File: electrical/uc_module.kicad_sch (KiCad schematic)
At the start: 36 parts, among them J1 Screw_Terminal_01x01, J6 Conn_01x06_Pin, K2 Starter RELAY, SW2 SW_SPST, SW3 NEUTRAL DETECT, SW4 KILL SWITCH, SW5 STARTER SWITCH, U1 ATtiny84A-PU, U2 LM7905

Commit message: Fixes in power module
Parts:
- removed D2: 1N4001, Diode_THT:D_DO-41_SOD81_P10.16mm_Horizontal, symbol Diode:1N4001
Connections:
- net POWER is gone; now on an unnamed net: F4.1
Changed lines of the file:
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@@
     (date "2023-03-26")
-  )
-  (junction (at 40.64 38.1) (diameter 0) (color 0 0 0 0)
   )
   (junction (at 52.07 124.46) (diameter 0) (color 0 0 0 0)
@@
     (stroke (width 0) (type default))
   )
-  (wire (pts (xy 43.18 49.53) (xy 40.64 49.53))
-    (stroke (width 0) (type default))
-  )
   (wire (pts (xy 68.58 87.63) (xy 77.47 87.63))
     (stroke (width 0) (type default))
@@
     (stroke (width 0) (type default))
   )
-  (wire (pts (xy 40.64 38.1) (xy 39.37 38.1))
+  (wire (pts (xy 29.21 38.1) (xy 50.8 38.1))
     (stroke (width 0) (type default))
   )
@@
     (stroke (width 0) (type default))
   )
-  (wire (pts (xy 40.64 38.1) (xy 40.64 49.53))
-    (stroke (width 0) (type default))
-  )
   (bus (pts (xy 80.01 92.71) (xy 80.01 95.25))
     (stroke (width 0) (type default))
@@
     (stroke (width 0) (type default))
   )
-  (wire (pts (xy 29.21 38.1) (xy 31.75 38.1))
-    (stroke (width 0) (type default))
-  )
   (wire (pts (xy 68.58 77.47) (xy 138.43 77.47))
     (stroke (width 0) (type default))
@@
   )
   (wire (pts (xy 214.63 71.12) (xy 214.63 102.87))
-    (stroke (width 0) (type default))
-  )
-  (wire (pts (xy 40.64 38.1) (xy 50.8 38.1))
     (stroke (width 0) (type default))
   )
@@
   (label "SCK" (at 69.85 87.63 0) (fields_autoplaced)
     (effects (font (size 1.27 1.27)) (justify left bottom))
-  )
-  (global_label "POWER" (shape bidirectional) (at 43.18 49.53 0) (fields_autoplaced)
-    (effects (font (size 1.27 1.27)) (justify left))
-    (property "Intersheetrefs" "${INTERSHEET_REFS}" (at 53.668 49.53 0)
-      (effects (font (size 1.27 1.27)) (justify left) hide)
-    )
   )
   (global_label "BULB STATUS" (shape input) (at 36.83 85.09 180) (fields_autoplaced)
@@
         )
       )
-    )
-  )
-  (symbol (lib_id "Diode:1N4001") (at 35.56 38.1 180) (unit 1)
-    (in_bom yes) (on_board yes) (dnp no)
-    (property "Reference" "D2" (at 35.56 43.18 0)
-      (effects (font (size 1.27 1.27)))
-    )
-    (property "Value" "1N4001" (at 35.56 40.64 0)
-      (effects (font (size 1.27 1.27)))
-    )
-    (property "Footprint" "Diode_THT:D_DO-41_SOD81_P10.16mm_Horizontal" (at 35.56 38.1 0)
-      (effects (font (size 1.27 1.27)) hide)
-    )
-    (property "Datasheet" "http://www.vishay.com/docs/88503/1n4001.pdf" (at 35.56 38.1 0)
-      (effects (font (size 1.27 1.27)) hide)
-    )
-    (property "Sim.Device" "D" (at 35.56 38.1 0)
-      (effects (font (size 1.27 1.27)) hide)
-    )
-    (property "Sim.Pins" "1=K 2=A" (at 35.56 38.1 0)
-      (effects (font (size 1.27 1.27)) hide)
-    )
-    (pin "1")
-    (pin "2")
-    (instances
-      (project "led_drive"
-        (path "/01e69042-7c7e-48e9-b7c3-459316fd17f1/111fb05e-7613-4dff-b0ef-7b688bb51755"
-          (reference "D2") (unit 1)
-        )
-      )

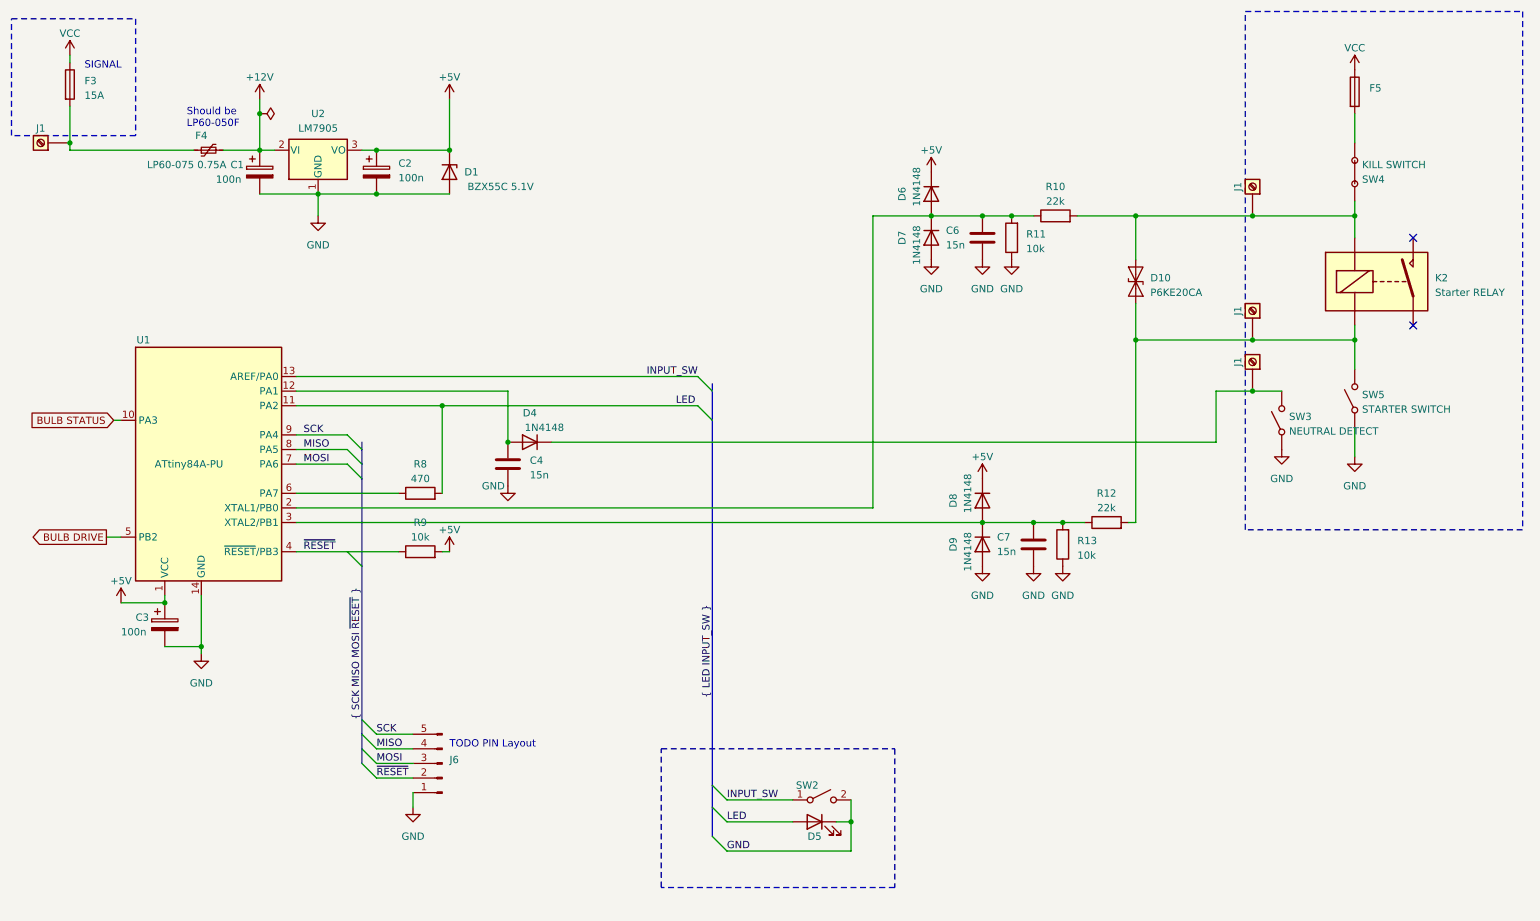
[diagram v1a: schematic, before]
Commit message: Added power module with MOSFET-N
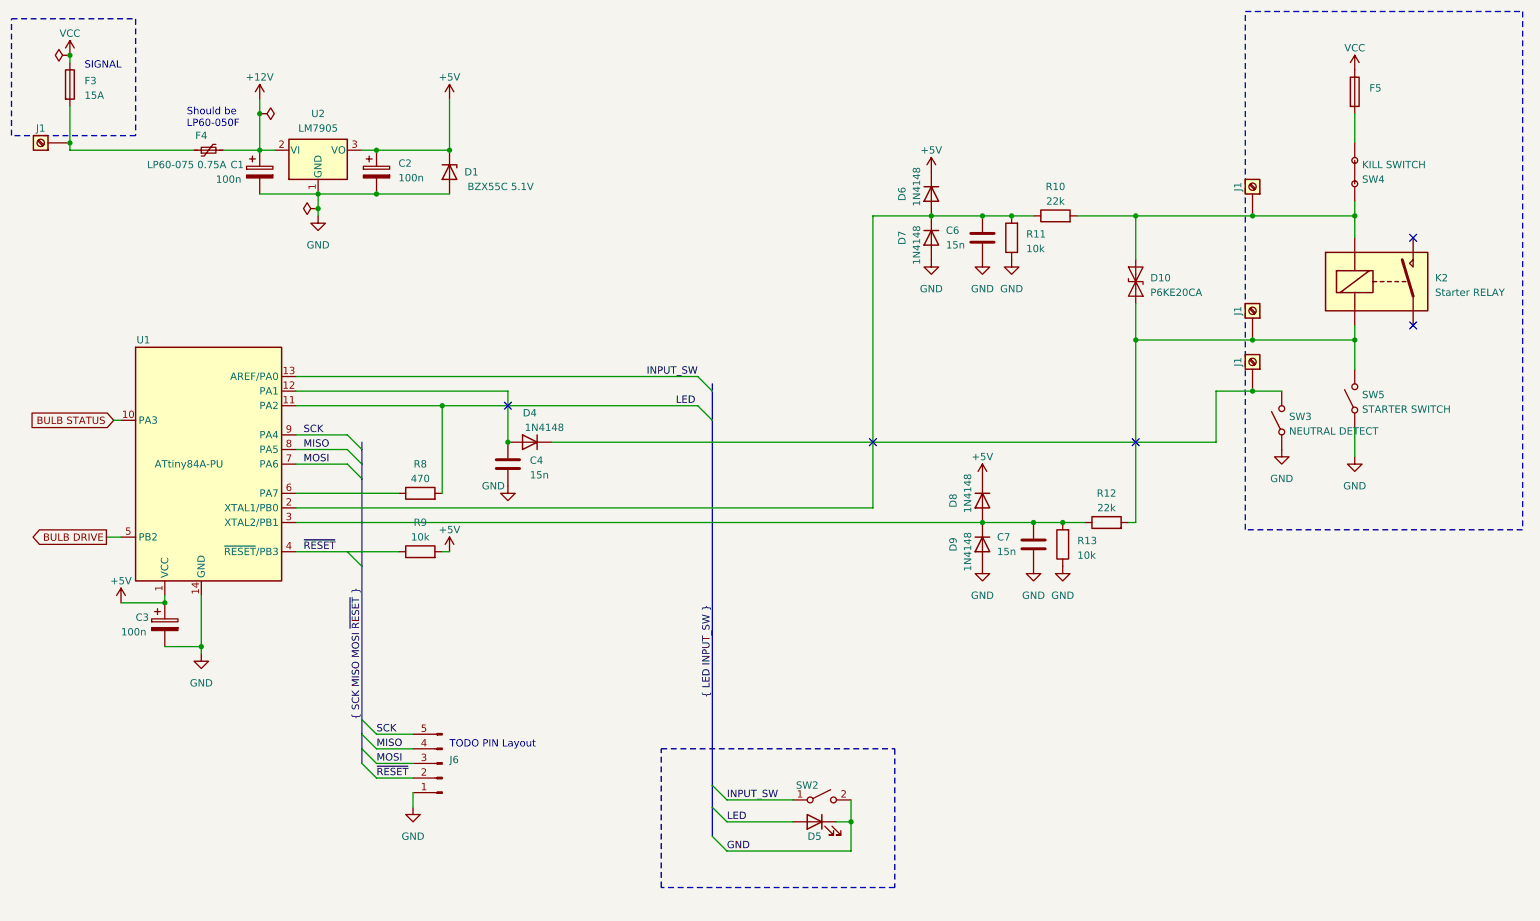
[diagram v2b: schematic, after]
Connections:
- no-connect marks 2 -> 5
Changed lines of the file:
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@@
     (date "2023-03-26")
   )
+  (junction (at 72.39 48.26) (diameter 0) (color 0 0 0 0)
+  )
   (junction (at 52.07 124.46) (diameter 0) (color 0 0 0 0)
   )
@@
   (junction (at 45.72 116.84) (diameter 0) (color 0 0 0 0)
   )
+  (junction (at 29.21 21.59) (diameter 0) (color 0 0 0 0)
+  )
   (junction (at 165.1 154.94) (diameter 0) (color 0 0 0 0)
   )
@@
   )
   (no_connect (at 262.89 53.34))
+  (no_connect (at 105.41 82.55))
+  (no_connect (at 168.91 88.9))
+  (no_connect (at 214.63 88.9))
   (no_connect (at 262.89 68.58))
   (bus_entry (at 80.01 137.16) (size 2.54 2.54)
@@
     (stroke (width 0) (type default))
   )
+  (wire (pts (xy 72.39 48.26) (xy 72.39 45.72))
+    (stroke (width 0) (type default))
+  )
   (wire (pts (xy 36.83 85.09) (xy 38.1 85.09))
     (stroke (width 0) (type default))
@@
     (stroke (width 0) (type default))
   )
-  (wire (pts (xy 72.39 49.53) (xy 72.39 45.72))
+  (wire (pts (xy 72.39 49.53) (xy 72.39 48.26))
     (stroke (width 0) (type default))
   )
@@
     )
   )
+  (symbol (lib_id "power:PWR_FLAG") (at 29.21 21.59 90) (unit 1)
+    (in_bom yes) (on_board yes) (dnp no) (fields_autoplaced)
+    (property "Reference" "#FLG04" (at 27.305 21.59 0)
+      (effects (font (size 1.27 1.27)) hide)
+    )
+    (property "Value" "PWR_FLAG" (at 25.4 22.225 90)
+      (effects (font (size 1.27 1.27)) (justify left) hide)
+    )
+    (property "Footprint" "" (at 29.21 21.59 0)
+      (effects (font (size 1.27 1.27)) hide)
+    )
+    (property "Datasheet" "~" (at 29.21 21.59 0)
+      (effects (font (size 1.27 1.27)) hide)
+    )
+    (property "Sim.Device" "V" (at 29.21 21.59 0)
+      (effects (font (size 1.27 1.27)) hide)
+    )
+    (property "Sim.Type" "DC" (at 29.21 21.59 0)
+      (effects (font (size 1.27 1.27)) hide)
+    )
+    (property "Sim.Pins" "1=+" (at 29.21 21.59 0)
+      (effects (font (size 1.27 1.27)) hide)
+    )
+    (property "Sim.Params" "dc=12" (at 29.21 21.59 0)
+      (effects (font (size 1.27 1.27)) hide)
+    )
+    (pin "1")
+    (instances
+      (project "led_drive"
+        (path "/01e69042-7c7e-48e9-b7c3-459316fd17f1/111fb05e-7613-4dff-b0ef-7b688bb51755"
+          (reference "#FLG04") (unit 1)
+        )
+      )
+    )
+  )
   (symbol (lib_id "power:GND") (at 187.96 110.49 0) (unit 1)
     (in_bom yes) (on_board yes) (dnp no) (fields_autoplaced)
@@
         )
       )
+    )
+  )
+  (symbol (lib_id "power:PWR_FLAG") (at 72.39 48.26 90) (unit 1)
+    (in_bom yes) (on_board yes) (dnp no) (fields_autoplaced)
+    (property "Reference" "#FLG02" (at 70.485 48.26 0)
+      (effects (font (size 1.27 1.27)) hide)
+    )
+    (property "Value" "PWR_FLAG" (at 68.58 48.895 90)
+      (effects (font (size 1.27 1.27)) (justify left) hide)
+    )
+    (property "Footprint" "" (at 72.39 48.26 0)
+      (effects (font (size 1.27 1.27)) hide)
+    )
+    (property "Datasheet" "~" (at 72.39 48.26 0)
+      (effects (font (size 1.27 1.27)) hide)
+    )
+    (property "Sim.Device" "V" (at 72.39 48.26 0)
+      (effects (font (size 1.27 1.27)) hide)
+    )
+    (property "Sim.Type" "DC" (at 72.39 48.26 0)
+      (effects (font (size 1.27 1.27)) hide)
+    )
+    (property "Sim.Pins" "1=+" (at 72.39 48.26 0)
+      (effects (font (size 1.27 1.27)) hide)
+    )
+    (property "Sim.Params" "dc=0" (at 72.39 48.26 0)
+      (effects (font (size 1.27 1.27)) hide)
+    )
+    (pin "1")
+    (instances
+      (project "led_drive"
+        (path "/01e69042-7c7e-48e9-b7c3-459316fd17f1/111fb05e-7613-4dff-b0ef-7b688bb51755"
+          (reference "#FLG02") (unit 1)
+        )
+      )

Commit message: Updated according to recent changes
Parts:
- removed D1: BZX55C 5.1V, Diode_THT:D_DO-35_SOD27_P7.62mm_Horizontal, symbol Diode:BZX84Cxx
- removed D6, D8: 1N4148, Diode_THT:D_DO-35_SOD27_P7.62mm_Horizontal, symbol Diode:1N4148
- removed F4: LP60-075 0.75A, Diode_THT:D_DO-35_SOD27_P12.70mm_Horizontal, symbol Device:Polyfuse_Small
- added C9: 15n, symbol Device:C
- added D1 (x2): BZX55C 4.7V, Diode_THT:D_DO-35_SOD27_P7.62mm_Horizontal, symbol Diode:BZX84Cxx
- added D13: 1N4148, Diode_THT:D_DO-35_SOD27_P7.62mm_Horizontal, symbol Diode:1N4148
- added D8: 1N4002, Diode_THT:D_DO-41_SOD81_P10.16mm_Horizontal, symbol Diode:1N4002
- C1: value 100n -> 200n
- R9: value 10k -> 12k
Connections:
- net GND: now also J6.2 (Pin_2), C9.2, D1.1 (A), D1.1 (A), D13.2 (A); no longer D7.2 (A), D9.2 (A), J6.1 (Pin_1)
- net INPUT_SW: now also C9.1
- net MISO: now also J6.5 (Pin_5); no longer J6.4 (Pin_4)
- net MOSI: now also J6.4 (Pin_4); no longer J6.3 (Pin_3)
- net SCK: now also J6.3 (Pin_3); no longer J6.5 (Pin_5)
- net ~{RESET}: now also J6.1 (Pin_1); no longer J6.2 (Pin_2)
- net at D10.1 (A1), J1.1 (Pin_1), K2.3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: now also D9.2 (A); no longer R12.2
- net at D10.2 (A2), J1.1 (Pin_1), K2.5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: now also D7.2 (A); no longer R10.2
- net STARTER: now reaches C7.1, R12.1, R13.2, U1.3 (XTAL2/PB1)
- net STARTER: now also D1.3 (K); no longer D9.1 (K)
- net at F3.2, J1.1 (Pin_1): now also D8.2 (A)
- net IGNITION: now reaches C6.1, R10.1, R11.2, U1.2 (XTAL1/PB0)
- net IGNITION: now also D1.3 (K); no longer D7.1 (K)
- net at D4.1 (K), J1.1 (Pin_1), SW3.2 (B): now also D13.1 (K)
- net NEUTRAL: now reaches C4.1, D4.2 (A), U1.12 (PA1)
- net LED_OUT: now reaches R8.1, U1.6 (PA7)
- net BULB DRIVE renamed BEAM_OUT
- net BULB STATUS renamed BEAM_IN
- net VDC renamed POWER_12
- net POWER_12: now also D8.1 (K)
- new net: D9.1 (K), R12.2
- new net: D7.1 (K), R10.2
- no-connect marks 5 -> 2
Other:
- note added: "Depending on LED used"
- note added: "Those two lines are interchangeable"
- note removed: "Should be LP60-050F"
- note removed: "TODO PIN Layout"
- moved on the sheet: C1, C2, C4, D4, D5, D7, D9, J6, SW2, U2

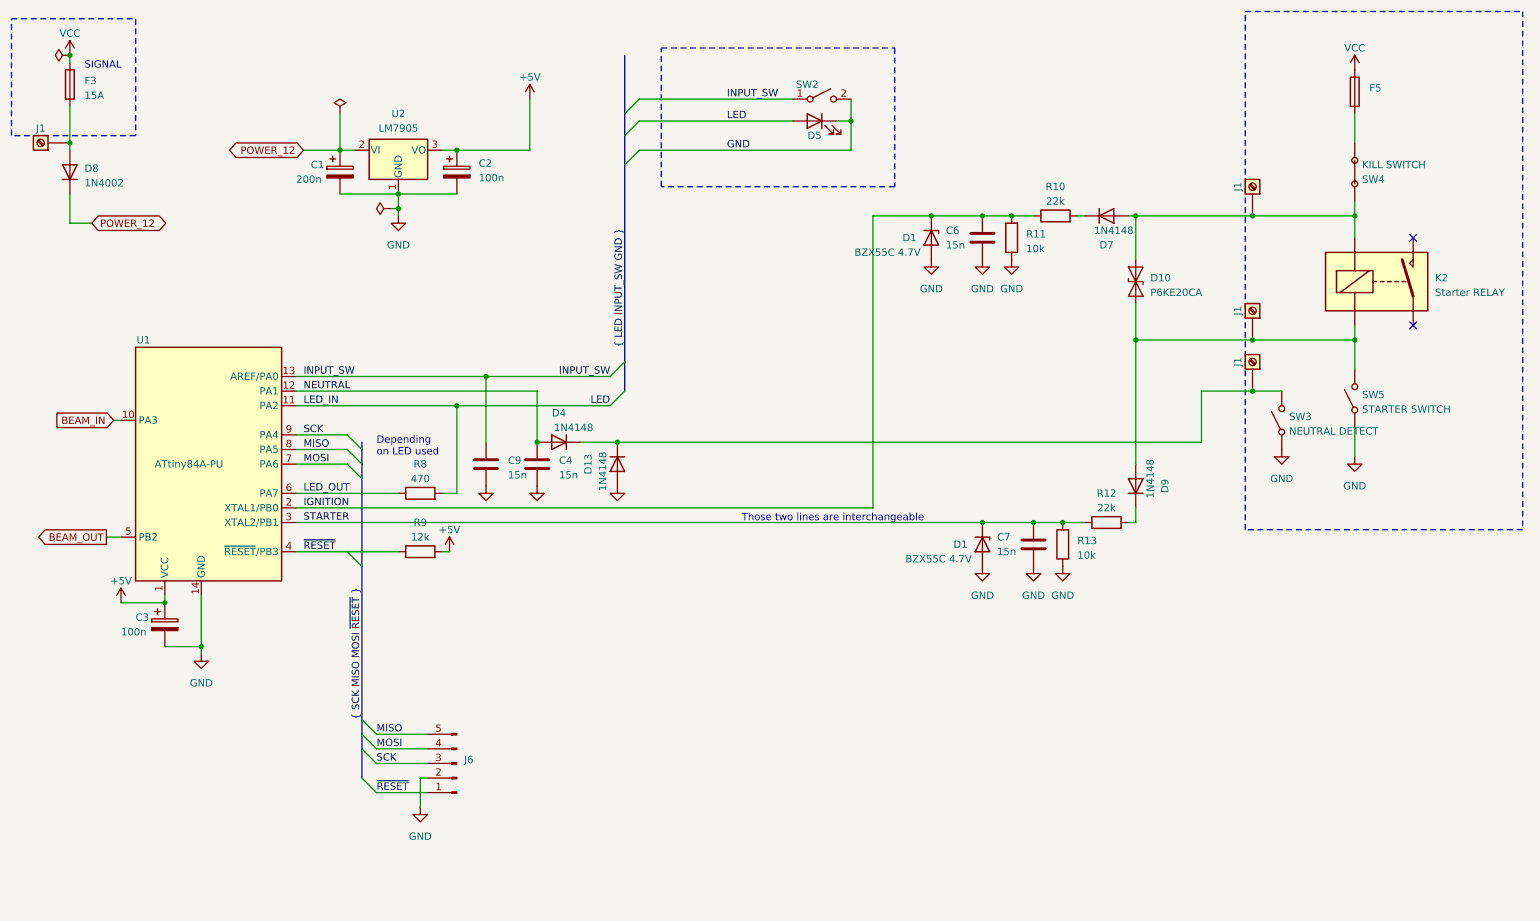
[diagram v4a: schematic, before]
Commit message: Electrical diagram refactor
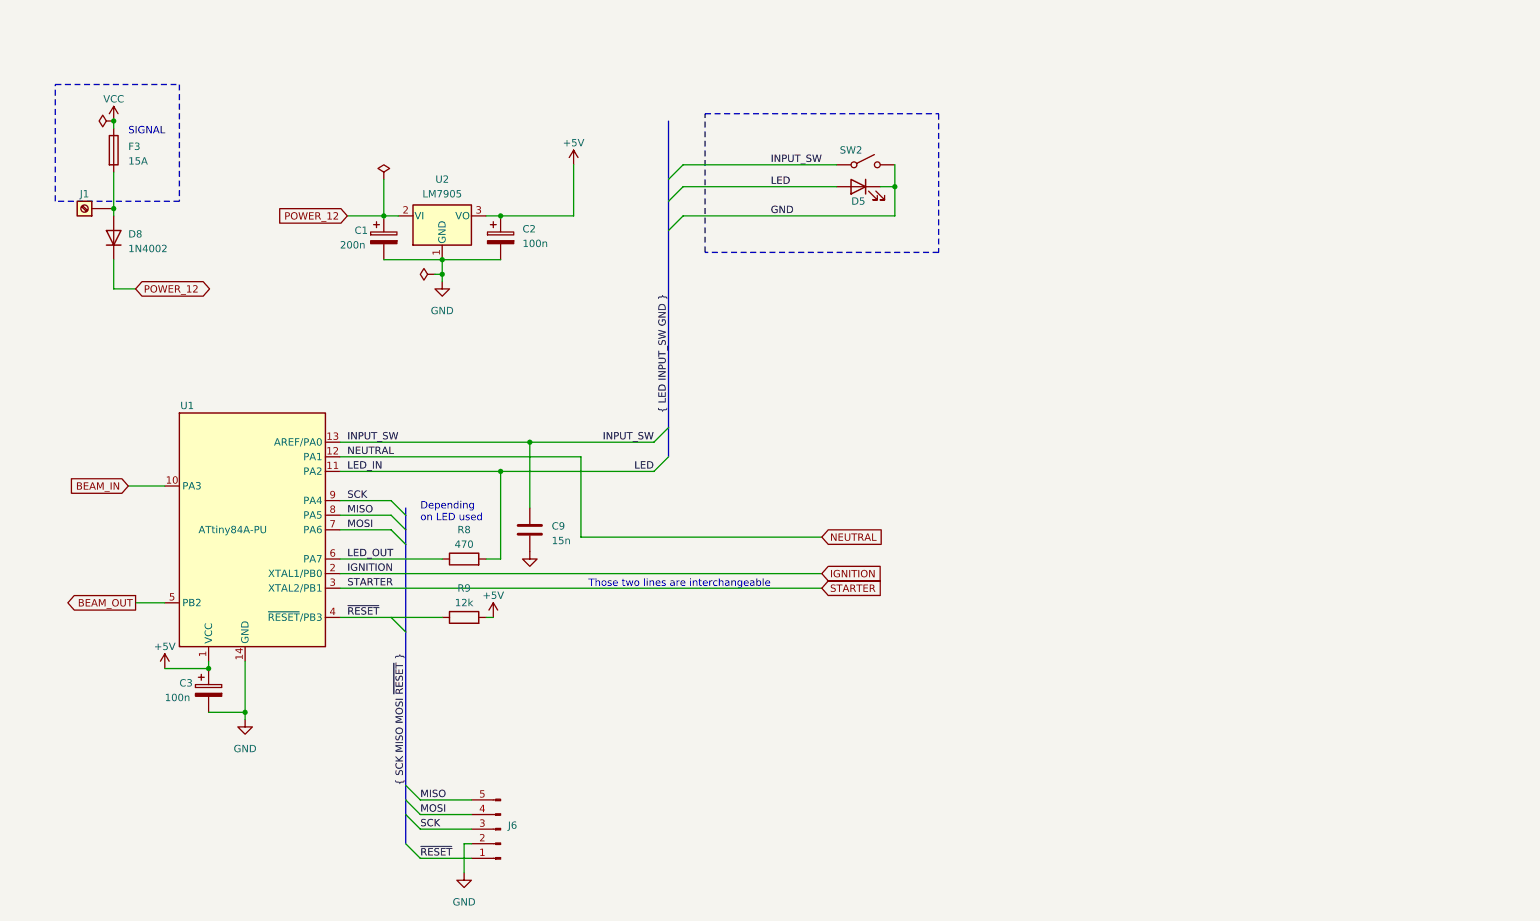
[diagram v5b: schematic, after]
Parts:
- removed C4, C6, C7: 15n, symbol Device:C
- removed D1 (x2): BZX55C 4.7V, Diode_THT:D_DO-35_SOD27_P7.62mm_Horizontal, symbol Diode:BZX84Cxx
- removed D10: P6KE20CA, Diode_THT:D_DO-15_P12.70mm_Horizontal, symbol Diode:SD15_SOD323
- removed D13, D4, D7, D9: 1N4148, Diode_THT:D_DO-35_SOD27_P7.62mm_Horizontal, symbol Diode:1N4148
- removed F5: ~, symbol Device:Fuse
- removed J1 (x3): Screw_Terminal_01x01, symbol Connector:Screw_Terminal_01x01
- removed K2: Starter RELAY, Relay_THT:Relay_SPST_StandexMeder_SIL_Form1A, symbol Relay:SILxx-1Axx-71x
- removed R10, R12: 22k, symbol Device:R
- removed R11, R13: 10k, symbol Device:R
- removed SW3: NEUTRAL DETECT, symbol Switch:SW_SPST
- removed SW4: KILL SWITCH, symbol Switch:SW_SPST
- removed SW5: STARTER SWITCH, symbol Switch:SW_SPST
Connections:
- no-connect marks 2 -> 0
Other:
- moved on the sheet: C1, C2, C3, C9, D5, D8, F3, J1, J6, R8, R9, U1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

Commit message: electrical module draft
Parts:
- removed C1: 200n, Diode_THT:D_DO-35_SOD27_P7.62mm_Horizontal, symbol Device:C_Polarized
- removed C2: 100n, Diode_THT:D_DO-35_SOD27_P7.62mm_Horizontal, symbol Device:C_Polarized
- removed D8: 1N4002, Diode_THT:D_DO-41_SOD81_P10.16mm_Horizontal, symbol Diode:1N4002
- removed F3: 15A, symbol Device:Fuse
- removed J1: Screw_Terminal_01x01, symbol Connector:Screw_Terminal_01x01
- removed U2: LM7905, Package_TO_SOT_THT:TO-220-3_Vertical, symbol Regulator_Linear:LM7905_TO220
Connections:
- net BEAM_IN renamed POWER_SENSE
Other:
- note removed: "SIGNAL"

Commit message: Work in progress
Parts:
- added D4: GREEN, symbol Device:LED
- added R10: 470, symbol Device:R
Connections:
- net STARTER is gone; now on net NEUTRAL: U1.3 (XTAL2/PB1)
- net +5V: now also D4.2 (A)
- net LED: no longer U1.11 (PA2)
- net NEUTRAL: no longer U1.12 (PA1)
- net POWER_SENSE: now also U1.11 (PA2); no longer U1.10 (PA3)
- net BEAM_OUT renamed BULB_OUT
- net IGNITION renamed OLI PRESSURE
- net OLI PRESSURE: now also R10.1
- new net: D4.1 (K), R10.2
- new net BULB_SENSE: U1.10 (PA3)
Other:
- note removed: "Those two lines are interchangeable"
- moved on the sheet: C9, J6, R8, R9
